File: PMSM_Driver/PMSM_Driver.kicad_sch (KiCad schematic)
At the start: 286 parts, among them J1 2606-1101, J10 HFBR-2521Z, J11 HFBR-2521Z, J12 HFBR-2521Z, J13 HFBR-2521Z, J14 HFBR-2521Z, J15 HFBR-2521Z, J16 HFBR-2521Z, J17 2606-1101, J18 2606-1101, J2 HFBR-2521Z, J3 1714971, J4 1714971, J5 1827907, J6 HFBR-2521Z, J7 HFBR-2521Z, J8 HFBR-2521Z, J9 HFBR-2521Z, Q1 BC846, Q10 BC846, Q11 RGCL60TK60, Q12 RGCL60TK60, Q13 RGCL60TK60, Q14 RGCL60TK60, Q15 BC846, Q16 RGCL60TK60, Q17 RGCL60TK60, Q18 RGCL60TK60, Q19 RGCL60TK60, Q2 BC846, Q20 BC846, Q21 BC846, Q22 BC846, Q23 BC846, Q24 BC846, Q3 BC846, Q4 BC846, Q5 RGCL60TK60, Q6 RGCL60TK60, Q7 RGCL60TK60, Q8 RGCL60TK60, Q9 BC846, U1 74LVC1G04, U10 HCPL-3120, U11 HCPL-3120, U12 HCPL-3120, U13 74LVC1G04, U14 74LVC1G04, U15 74LVC1G04, U16 MGJ2D051515SC, U17 MGJ2D051515SC, U18 MGJ2D051515SC, U19 HCPL-3120, U2 MGJ2D051515SC, U20 HCPL-3120, U21 HCPL-3120, U22 74LVC1G04, U23 74LVC1G04, U24 74LVC1G04, U25 MGJ2D051515SC, U26 MGJ2D051515SC, U27 MGJ2D051515SC, U28 HCPL-3120, U29 HCPL-3120, U3 HCPL-3120, U30 HCPL-3120, U31 74LVC1G04, U32 74LVC1G04, U33 MGJ2D051515SC, U34 MGJ2D051515SC, U35 HCPL-3120, U36 HCPL-3120, U37 VS-E5TH3006S2L-M3, U38 VS-E5TH3006S2L-M3, U39 VS-E5TH3006S2L-M3, U4 74LVC1G04, U40 VS-E5TH3006S2L-M3, U41 VS-E5TH3006S2L-M3, U42 VS-E5TH3006S2L-M3, U43 VS-E5TH3006S2L-M3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

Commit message: Final Version 1 Update
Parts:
- added C95, C96, C97: 1n, Capacitor_SMD:C_1206_3216Metric, symbol Device:C_Polarized
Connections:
- net GND: now also C95.2, C96.2, C97.2
- net at C84.1, U57.7 (VIOUT), U60.3 (VIN+): now also C97.1
- net at C82.1, U55.7 (VIOUT), U58.3 (VIN+): now also C95.1
- net at C83.1, U56.7 (VIOUT), U59.3 (VIN+): now also C96.1
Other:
- note added: "3-Phase Diode-Clamped Three-Level Inverter"
- note removed: "Power Supply"
- note removed: "Three Phase Inverter"
- moved on the sheet: C1, C2, C3, C4, C5, C6, C85, C86, C87, C88, C89, C9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

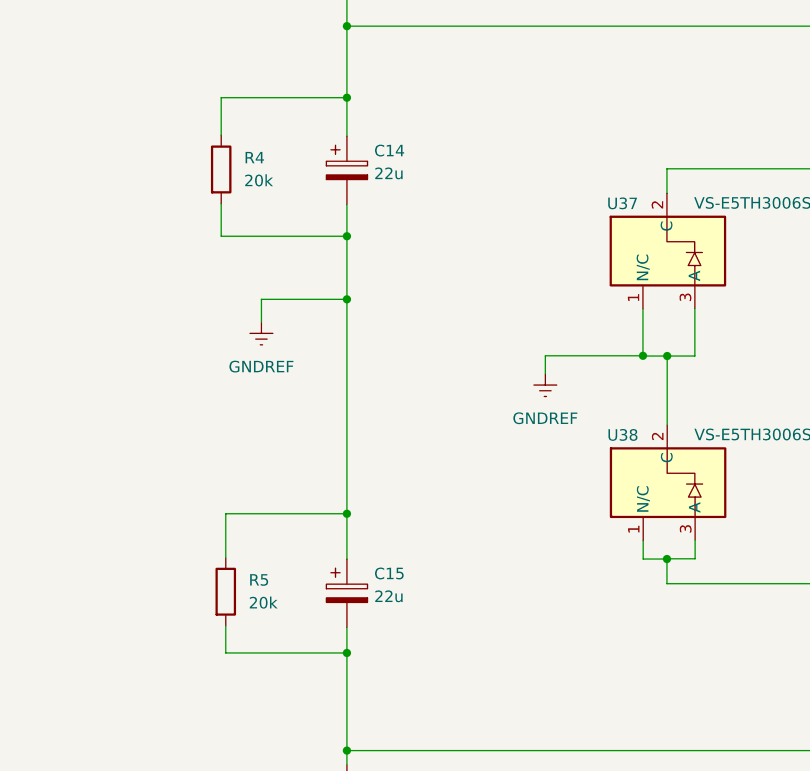
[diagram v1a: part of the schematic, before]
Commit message: Completed Version 2: changed the DC-link capacitance to 2200 uF
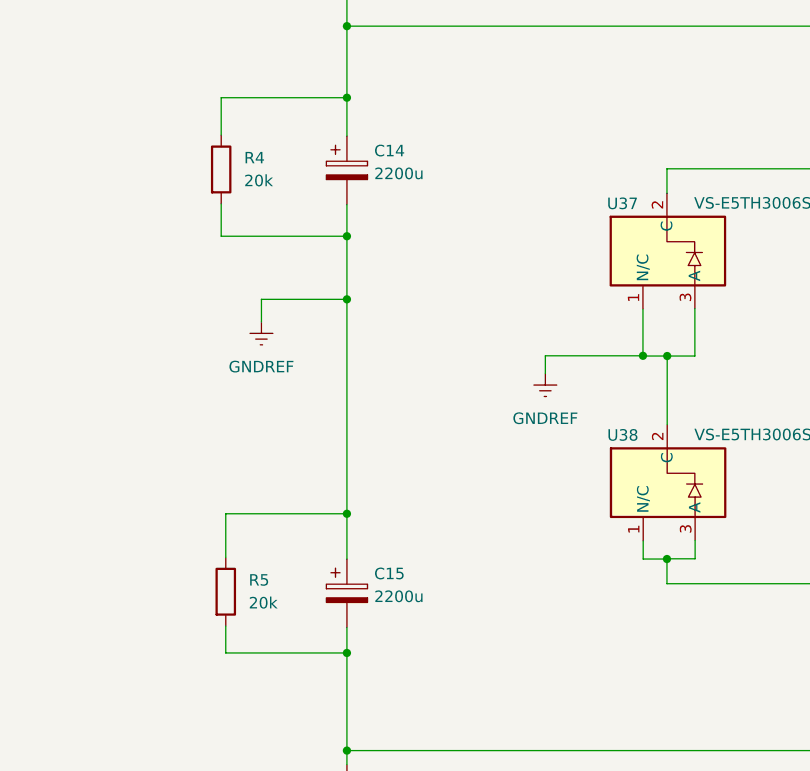
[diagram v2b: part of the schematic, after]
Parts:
- C14, C15: value 22u -> 2200u; footprint Capacitor_SMD:CP_Elec_16x17.5 -> FYP_Components:DC-link_ALC80C222FP400
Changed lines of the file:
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@@
       (effects (font (size 1.27 1.27)) (justify left))
     )
-    (property "Value" "22u" (at 101.2952 118.2369 0)
+    (property "Value" "2200u" (at 101.2952 118.2369 0)
       (effects (font (size 1.27 1.27)) (justify left))
     )
-    (property "Footprint" "Capacitor_SMD:CP_Elec_16x17.5" (at 99.2378 121.666 0)
+    (property "Footprint" "FYP_Components:DC-link_ALC80C222FP400" (at 99.2378 121.666 0)
       (effects (font (size 1.27 1.27)) hide)
     )
-    (property "Datasheet" "~" (at 98.2726 117.856 0)
+    (property "Datasheet" "https://search.kemet.com/download/specsheet/ALC80C222FP400" (at 98.2726 117.856 0)
       (effects (font (size 1.27 1.27)) hide)
     )
@@
       (effects (font (size 1.27 1.27)) (justify left))
     )
-    (property "Value" "22u" (at 101.2952 165.2269 0)
+    (property "Value" "2200u" (at 101.2952 165.2269 0)
       (effects (font (size 1.27 1.27)) (justify left))
     )
-    (property "Footprint" "Capacitor_SMD:CP_Elec_16x17.5" (at 99.2378 168.656 0)
+    (property "Footprint" "FYP_Components:DC-link_ALC80C222FP400" (at 99.2378 168.656 0)
       (effects (font (size 1.27 1.27)) hide)
     )
-    (property "Datasheet" "~" (at 98.2726 164.846 0)
+    (property "Datasheet" "https://search.kemet.com/download/specsheet/ALC80C222FP400" (at 98.2726 164.846 0)
       (effects (font (size 1.27 1.27)) hide)
     )

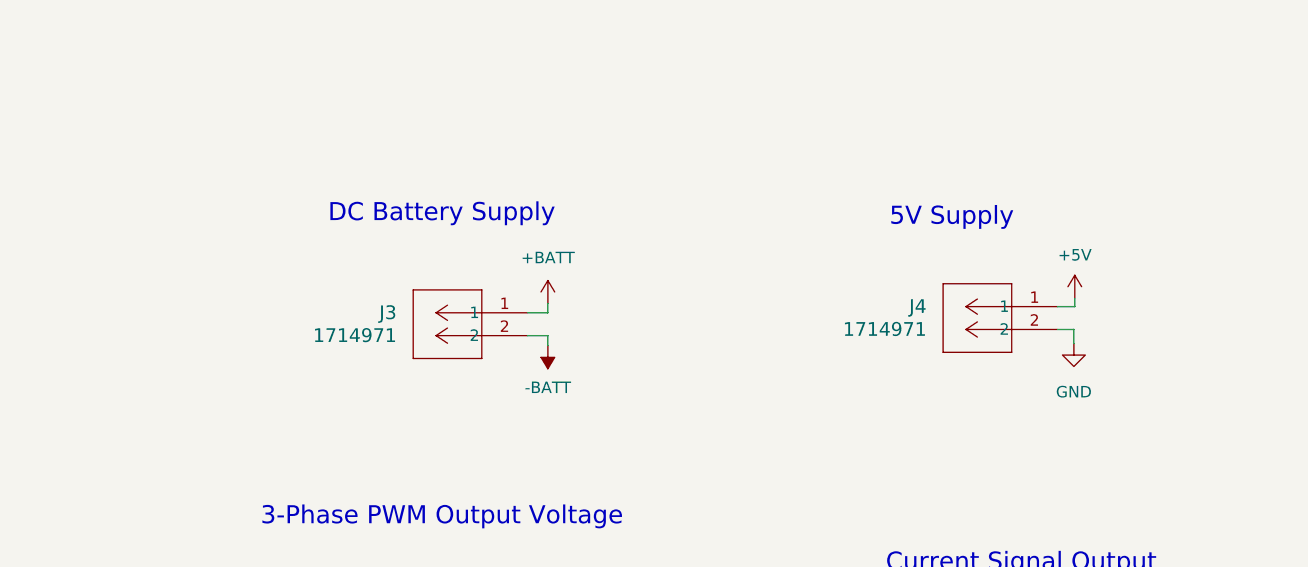
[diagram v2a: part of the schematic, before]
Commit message: CCS project is added, PCB layout are updated, simulations are combined into one file, the completed version of c-script simulation is to be done.
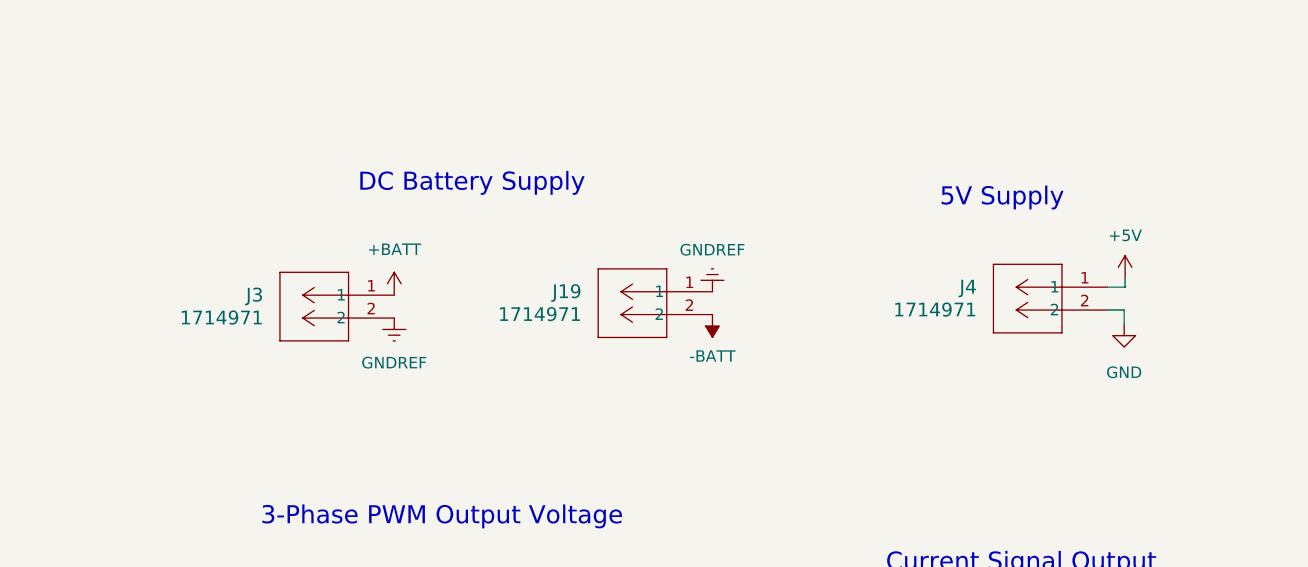
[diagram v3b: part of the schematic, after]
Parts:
- added J19: 1714971, FYP_Components:CONN_1714971_PXC, symbol FYP_Components:1714971
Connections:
- net -BATT: now also J19.2; no longer J3.2
- net GNDREF: now also J3.2, J19.1
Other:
- moved on the sheet: J3, J4

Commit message: updated thesis: 6th May
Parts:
- removed U1, U13, U14, U15, U22, U23, U24, U31, U32, U4, U5, U6: 74LVC1G04, Package_TO_SOT_SMD:SOT-23-5, symbol 74xGxx:74LVC1G04
- added U1, U13, U14, U15, U22, U23, U24, U31, U32, U4, U5, U6: SN74LV1T34DBV, Package_TO_SOT_SMD:SOT-23-5, symbol Logic_LevelTranslator:SN74LV1T34DBV
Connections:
- net +5V: now also U1.5 (VCC), U13.5 (VCC), U14.5 (VCC), U15.5 (VCC), U22.5 (VCC), U23.5 (VCC), U24.5 (VCC), U31.5 (VCC), U32.5 (VCC), U4.5 (VCC), U5.5 (VCC), U6.5 (VCC)
- net GND: now also U1.3 (GND), U13.3 (GND), U14.3 (GND), U15.3 (GND), U22.3 (GND), U23.3 (GND), U24.3 (GND), U31.3 (GND), U32.3 (GND), U4.3 (GND), U5.3 (GND), U6.3 (GND)
- net at J11.1 (Data_Out), J11.4 (Data_Out): now also U23.2 (A)
- net at J10.1 (Data_Out), J10.4 (Data_Out): now also U6.2 (A)
- net at R8.1: now also U6.4 (Y)
- net at J16.1 (Data_Out), J16.4 (Data_Out): now also U24.2 (A)
- net at J7.1 (Data_Out), J7.4 (Data_Out): now also U1.2 (A)
- net at R1.1: now also U1.4 (Y)
- net at J8.1 (Data_Out), J8.4 (Data_Out): now also U14.2 (A)
- net at R16.1: now also U14.4 (Y)
- net at J12.1 (Data_Out), J12.4 (Data_Out): now also U22.2 (A)
- net at R24.1: now also U22.4 (Y)
- net at J15.1 (Data_Out), J15.4 (Data_Out): now also U31.2 (A)
- net at R33.1: now also U31.4 (Y)
- net at J13.1 (Data_Out), J13.4 (Data_Out): now also U15.2 (A)
- net at R17.1: now also U15.4 (Y)
- net at J2.1 (Data_Out), J2.4 (Data_Out): now also U4.2 (A)
- net at R6.1: now also U4.4 (Y)
- net at J9.1 (Data_Out), J9.4 (Data_Out): now also U13.2 (A)
- net at R25.1: now also U23.4 (Y)
- net at R26.1: now also U24.4 (Y)
- net at R15.1: now also U13.4 (Y)
- net at R7.1: now also U5.4 (Y)
- net at R34.1: now also U32.4 (Y)
- net at J14.1 (Data_Out), J14.4 (Data_Out): now also U32.2 (A)
- net at J6.1 (Data_Out), J6.4 (Data_Out): now also U5.2 (A)
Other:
- note added: "Analogue Buffer"
- note added: "DC-DC Converter: 5V to +/- 15V"
- note added: "Digital Buffer"
- note added: "Isolated Gate Drive"
- note added: "Optical Receiver"
- note added: "Over-voltage Protection"
- note removed: "Voltage Follower"
- moved on the sheet: H1, H2, H3, H4, J1, J17, J18, J19, J3, J4, J5

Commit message: updated thesis: 8th May
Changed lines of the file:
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@@
     (stroke (width 0) (type default))
+  )
+  (text "Decoupling Capacitors" (at 265.6586 344.5002 0)
+    (effects (font (size 1.27 1.27) (thickness 0.254) bold) (justify left bottom))
   )
   (text "DC-DC Converter: 5V to +/- 15V" (at 207.6196 326.39 0)
